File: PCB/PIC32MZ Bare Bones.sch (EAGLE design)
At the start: 37 parts, among them U1 PIC32MZ2048EC(G/H/M)144-PL, U2 ADP3338AKCZ-3.3, X1 24MHz, Abracon ABM8, X2 32.768kHz

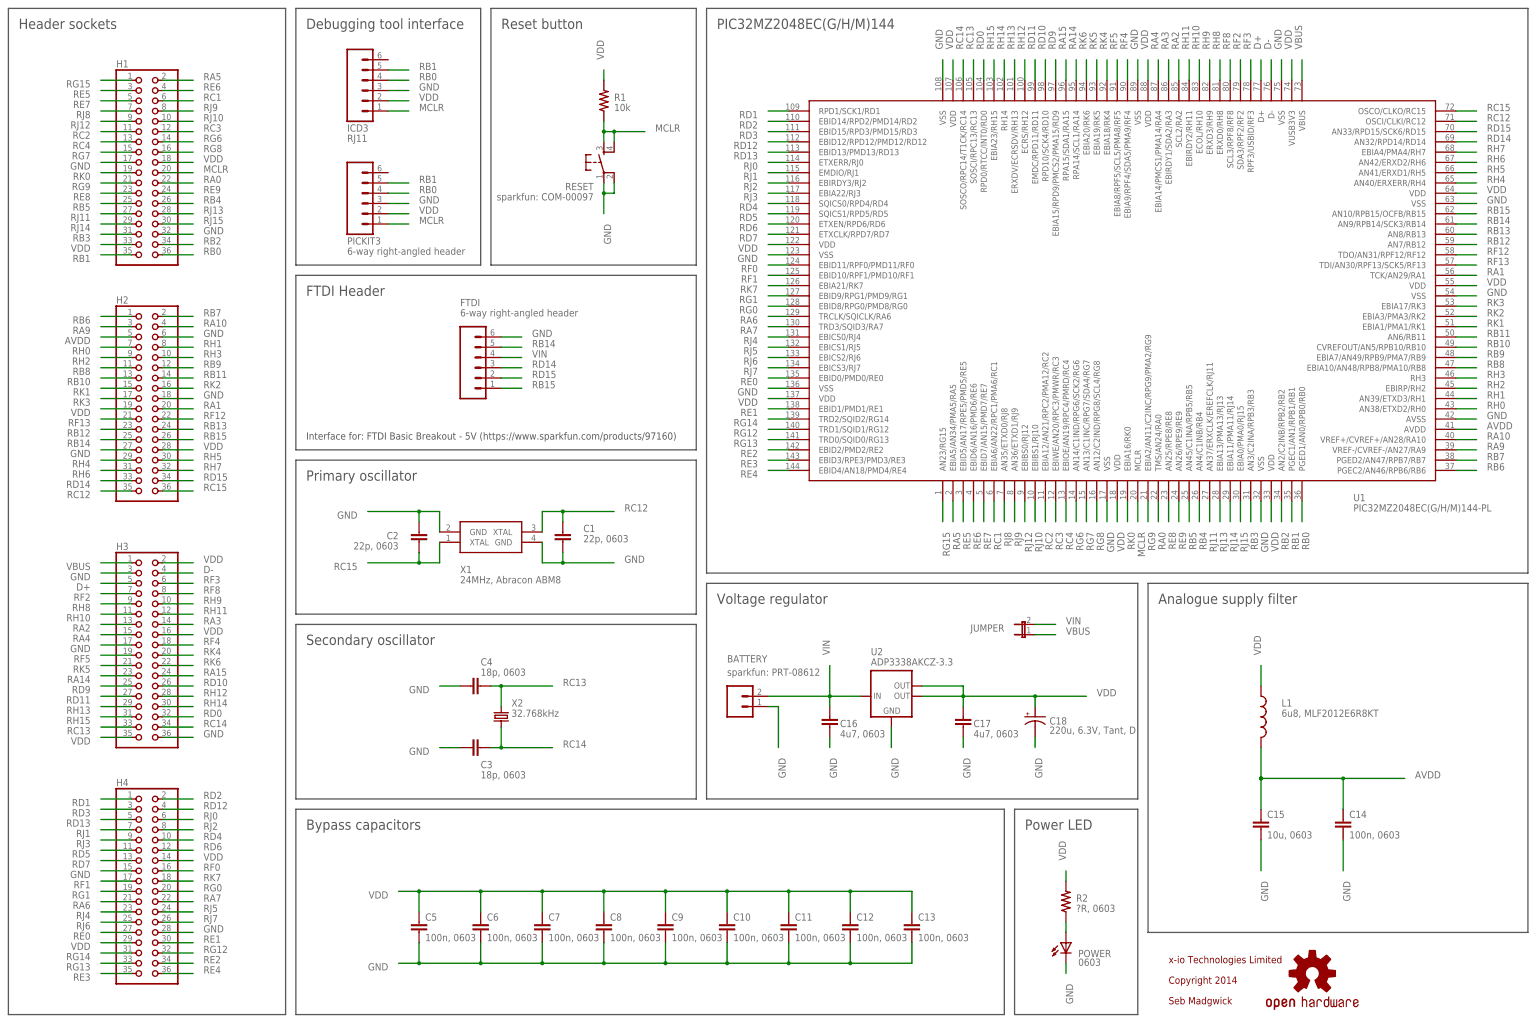
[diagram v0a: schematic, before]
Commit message: Remove battery, add USB host/device sockets
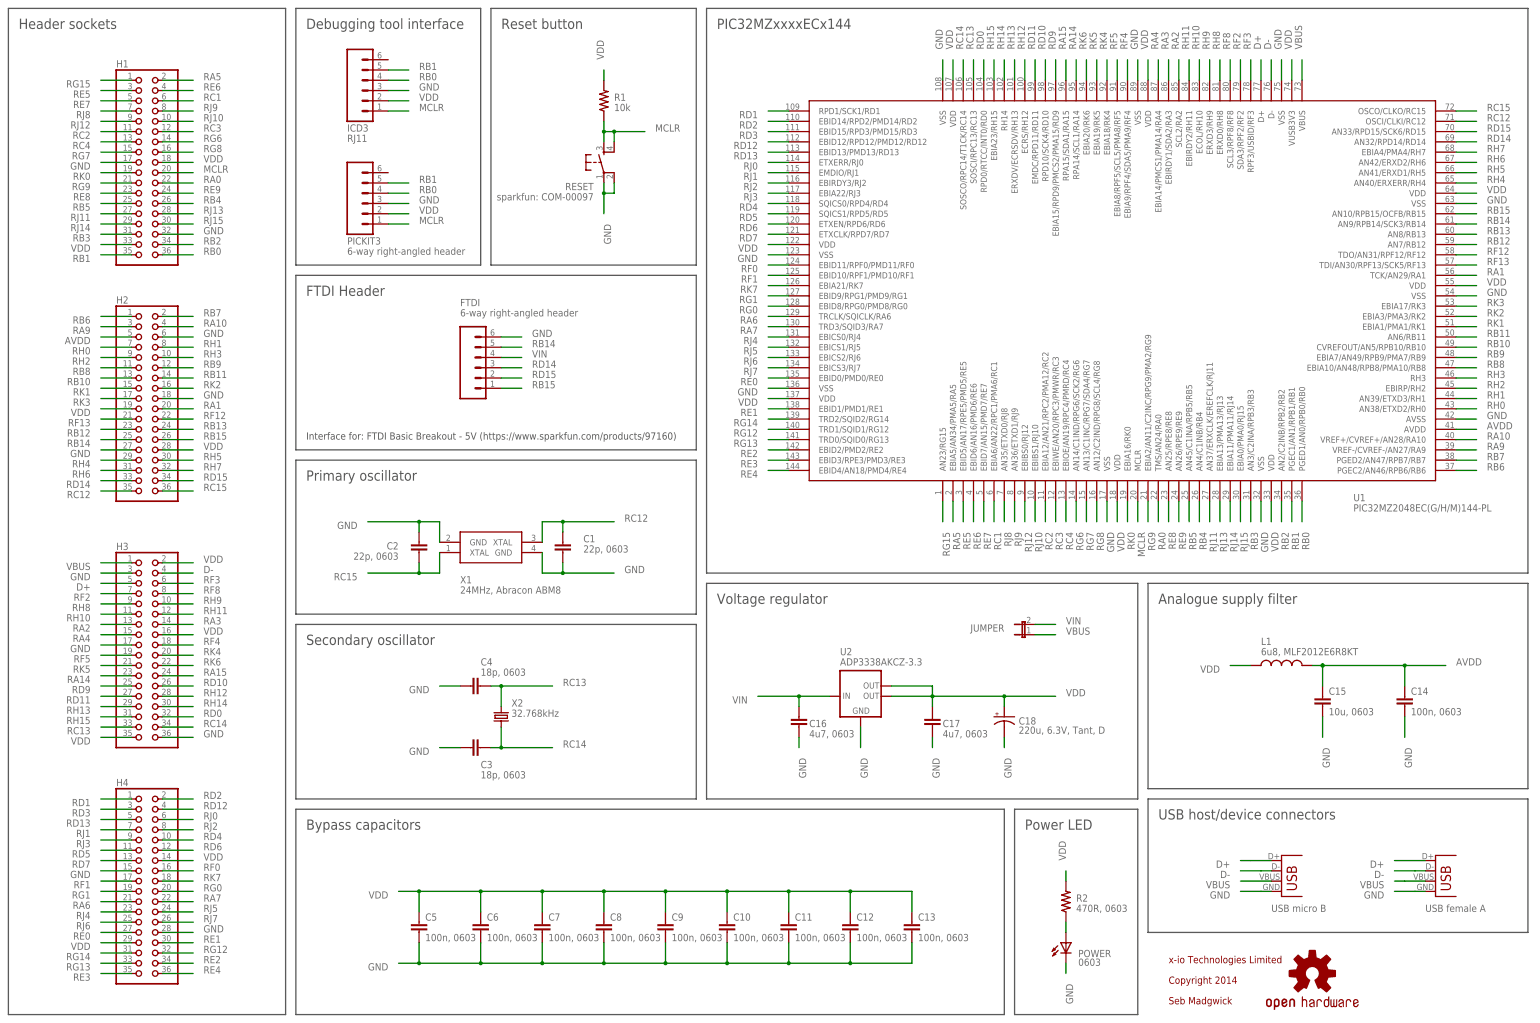
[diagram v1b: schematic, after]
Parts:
- removed BATTERY: sparkfun: PRT-08612, SparkFun:M02-JST-2MM-SMT
- added X3: USB-MICROB, SparkFun:USB-MICROB
- added X4: USB-A-SMD, SparkFun:USB-A-SMD
- R2: value ?R, 0603 -> 470R, 0603
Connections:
- net D+: now also X3.D+, X4.D+
- net D-: now also X3.D-, X4.D-
- net GND: now also X3.GND, X4.GND; no longer BATTERY.1
- net VBUS: now also X3.VBUS, X4.VBUS
- net VIN: no longer BATTERY.2
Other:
- note added: "PIC32MZxxxxECx144"
- note added: "USB female A"
- note added: "USB host/device connectors"
- note added: "USB micro B"
- note removed: "PIC32MZ2048EC(G/H/M)144"
- moved on the sheet: C1, C14, C15, C16, C17, C18, C2, L1, U2, X1

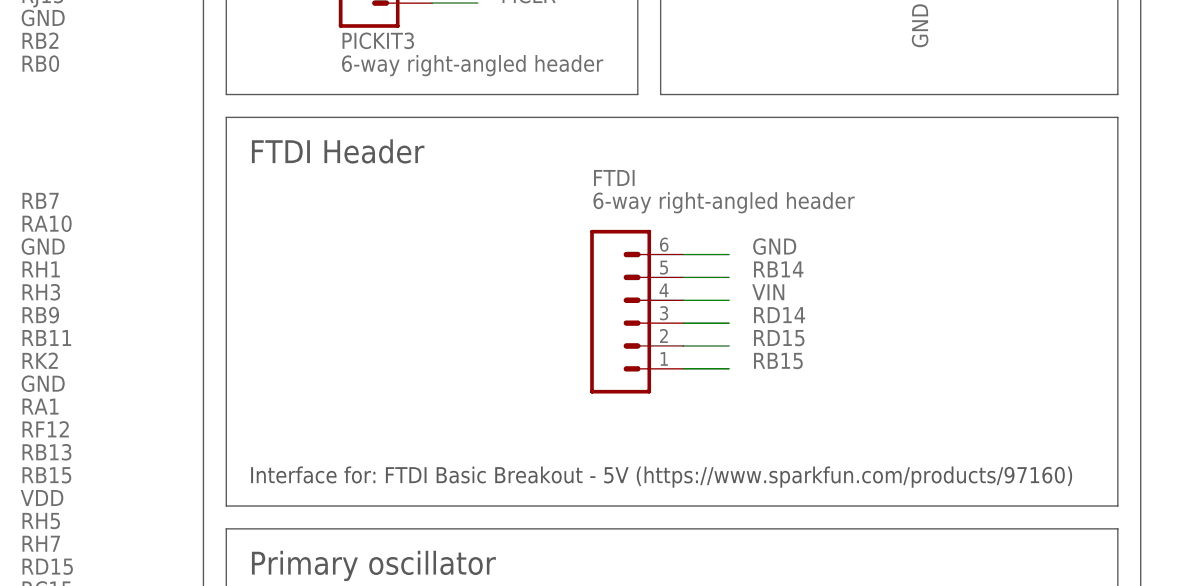
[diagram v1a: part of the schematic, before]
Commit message: 5V tolerance for FTDI inputs
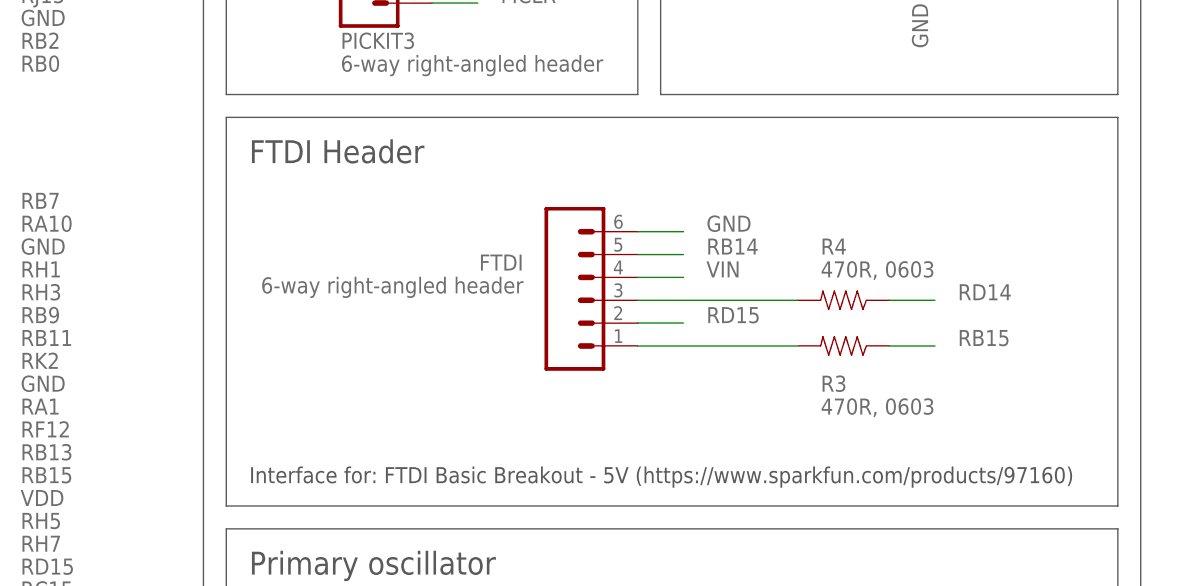
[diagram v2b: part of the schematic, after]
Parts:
- added R3, R4: 470R, 0603, SparkFun:RESISTOR0603-RES
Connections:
- new net N$1: FTDI.3, R4.2
- new net N$2: FTDI.1, R3.2
- net RB15: now also R3.1; no longer FTDI.1
- net RD14: now also R4.1; no longer FTDI.3
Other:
- moved on the sheet: FTDI
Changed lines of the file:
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@@
 <part name="X3" library="SparkFun" deviceset="USB" device="-MICROB"/>
 <part name="X4" library="SparkFun" deviceset="USB" device="-A-SMD"/>
+<part name="R3" library="SparkFun" deviceset="RESISTOR" device="0603-RES" value="470R, 0603"/>
+<part name="R4" library="SparkFun" deviceset="RESISTOR" device="0603-RES" value="470R, 0603"/>
 </parts>
 <sheets>
@@
 <attribute name="VALUE" x="154.94" y="228.6" size="1.778" layer="96"/>
 </instance>
-<instance part="FTDI" gate="G$1" x="121.92" y="165.1" smashed="yes">
-<attribute name="VALUE" x="116.84" y="177.8" size="1.778" layer="96"/>
-<attribute name="NAME" x="116.84" y="180.34" size="1.778" layer="95"/>
+<instance part="FTDI" gate="G$1" x="116.84" y="167.64" smashed="yes">
+<attribute name="VALUE" x="109.22" y="170.18" size="1.778" layer="96" rot="R180"/>
+<attribute name="NAME" x="109.22" y="172.72" size="1.778" layer="95" rot="R180"/>
 </instance>
 <instance part="POWER" gate="G$1" x="266.7" y="22.86" smashed="yes">
@@
 <instance part="X3" gate="G$1" x="320.04" y="35.56"/>
 <instance part="X4" gate="G$1" x="358.14" y="35.56"/>
+<instance part="R3" gate="G$1" x="144.78" y="162.56" smashed="yes" rot="R180">
+<attribute name="NAME" x="142.24" y="157.48" size="1.778" layer="95"/>
+<attribute name="VALUE" x="142.24" y="154.94" size="1.778" layer="96"/>
+</instance>
+<instance part="R4" gate="G$1" x="144.78" y="167.64" smashed="yes" rot="R180">
+<attribute name="NAME" x="142.24" y="172.72" size="1.778" layer="95"/>
+<attribute name="VALUE" x="142.24" y="170.18" size="1.778" layer="96"/>
+</instance>
 </instances>
 <busses>
@@
 <segment>
 <pinref part="FTDI" gate="G$1" pin="5"/>
-<wire x1="127" y1="170.18" x2="132.08" y2="170.18" width="0.1524" layer="91"/>
-<label x="134.62" y="170.18" size="1.778" layer="95"/>
+<wire x1="121.92" y1="172.72" x2="127" y2="172.72" width="0.1524" layer="91"/>
+<label x="129.54" y="172.72" size="1.778" layer="95"/>
 </segment>
 </net>
@@
 </segment>
 <segment>
-<pinref part="FTDI" gate="G$1" pin="1"/>
-<wire x1="127" y1="160.02" x2="132.08" y2="160.02" width="0.1524" layer="91"/>
-<label x="134.62" y="160.02" size="1.778" layer="95"/>
+<pinref part="R3" gate="G$1" pin="1"/>
+<wire x1="149.86" y1="162.56" x2="154.94" y2="162.56" width="0.1524" layer="91"/>
+<label x="157.48" y="162.56" size="1.778" layer="95"/>
 </segment>
 </net>
@@
 </segment>
 <segment>
-<pinref part="FTDI" gate="G$1" pin="3"/>
-<wire x1="127" y1="165.1" x2="132.08" y2="165.1" width="0.1524" layer="91"/>
-<label x="134.62" y="165.1" size="1.778" layer="95"/>
+<pinref part="R4" gate="G$1" pin="1"/>
+<wire x1="149.86" y1="167.64" x2="154.94" y2="167.64" width="0.1524" layer="91"/>
+<label x="157.48" y="167.64" size="1.778" layer="95"/>
 </segment>
 </net>
@@
 <segment>
 <pinref part="FTDI" gate="G$1" pin="2"/>
-<wire x1="127" y1="162.56" x2="132.08" y2="162.56" width="0.1524" layer="91"/>
-<label x="134.62" y="162.56" size="1.778" layer="95"/>
+<wire x1="121.92" y1="165.1" x2="127" y2="165.1" width="0.1524" layer="91"/>
+<label x="129.54" y="165.1" size="1.778" layer="95"/>
 </segment>
 </net>
@@
 <segment>
 <pinref part="FTDI" gate="G$1" pin="6"/>
-<wire x1="127" y1="172.72" x2="132.08" y2="172.72" width="0.1524" layer="91"/>
-<label x="134.62" y="172.72" size="1.778" layer="95"/>
+<wire x1="121.92" y1="175.26" x2="127" y2="175.26" width="0.1524" layer="91"/>
+<label x="129.54" y="175.26" size="1.778" layer="95"/>
 </segment>
 <segment>
@@
 <segment>
 <pinref part="FTDI" gate="G$1" pin="4"/>
-<wire x1="127" y1="167.64" x2="132.08" y2="167.64" width="0.1524" layer="91"/>
-<label x="134.62" y="167.64" size="1.778" layer="95"/>
+<wire x1="121.92" y1="170.18" x2="127" y2="170.18" width="0.1524" layer="91"/>
+<label x="129.54" y="170.18" size="1.778" layer="95"/>
 </segment>
 <segment>
@@
 </segment>
 </net>
+<net name="N$1" class="0">
+<segment>
+<pinref part="FTDI" gate="G$1" pin="3"/>
+<pinref part="R4" gate="G$1" pin="2"/>
+<wire x1="121.92" y1="167.64" x2="139.7" y2="167.64" width="0.1524" layer="91"/>
+</segment>
+</net>
+<net name="N$2" class="0">
+<segment>
+<pinref part="FTDI" gate="G$1" pin="1"/>
+<pinref part="R3" gate="G$1" pin="2"/>
+<wire x1="121.92" y1="162.56" x2="139.7" y2="162.56" width="0.1524" layer="91"/>
+</segment>
+</net>
